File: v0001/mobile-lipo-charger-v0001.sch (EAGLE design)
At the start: 76 parts, among them IC1 AD8610MR, IC3 AD8610MR, IC5 STM32F429NGH, SW2 DHT-4235A, U3 3.3V, U4 3.3V

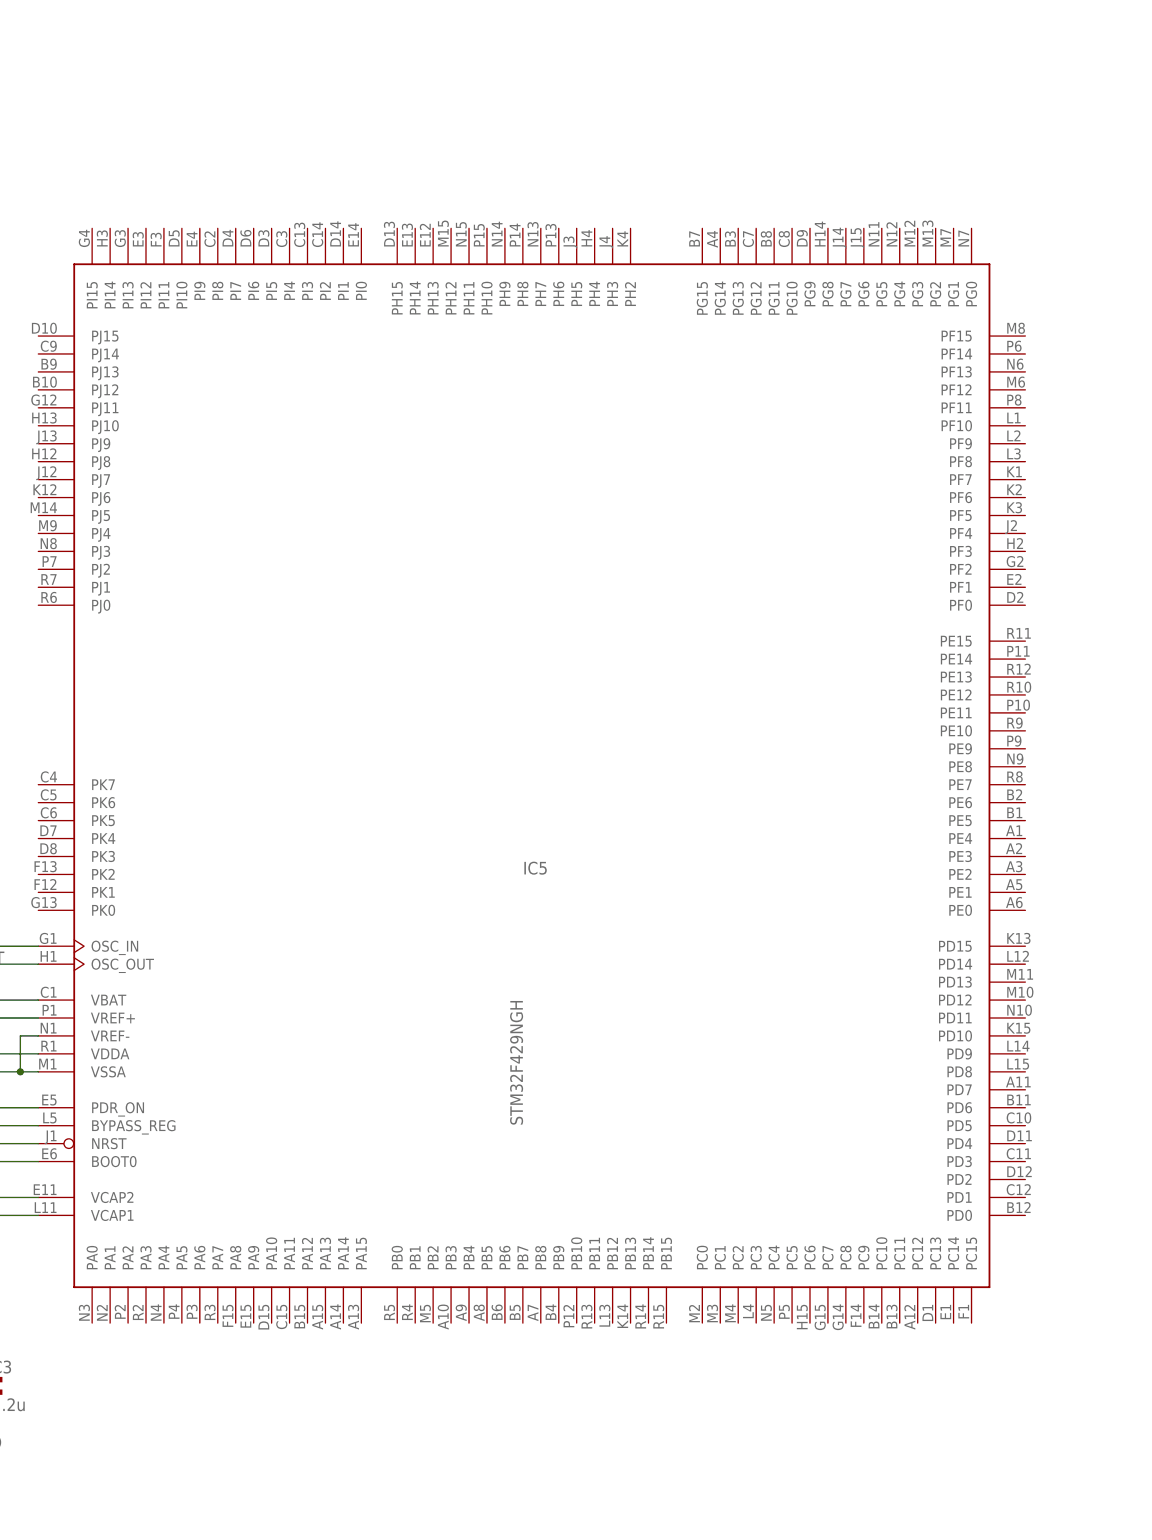
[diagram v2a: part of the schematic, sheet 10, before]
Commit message: Routing
Began routing TFT signals
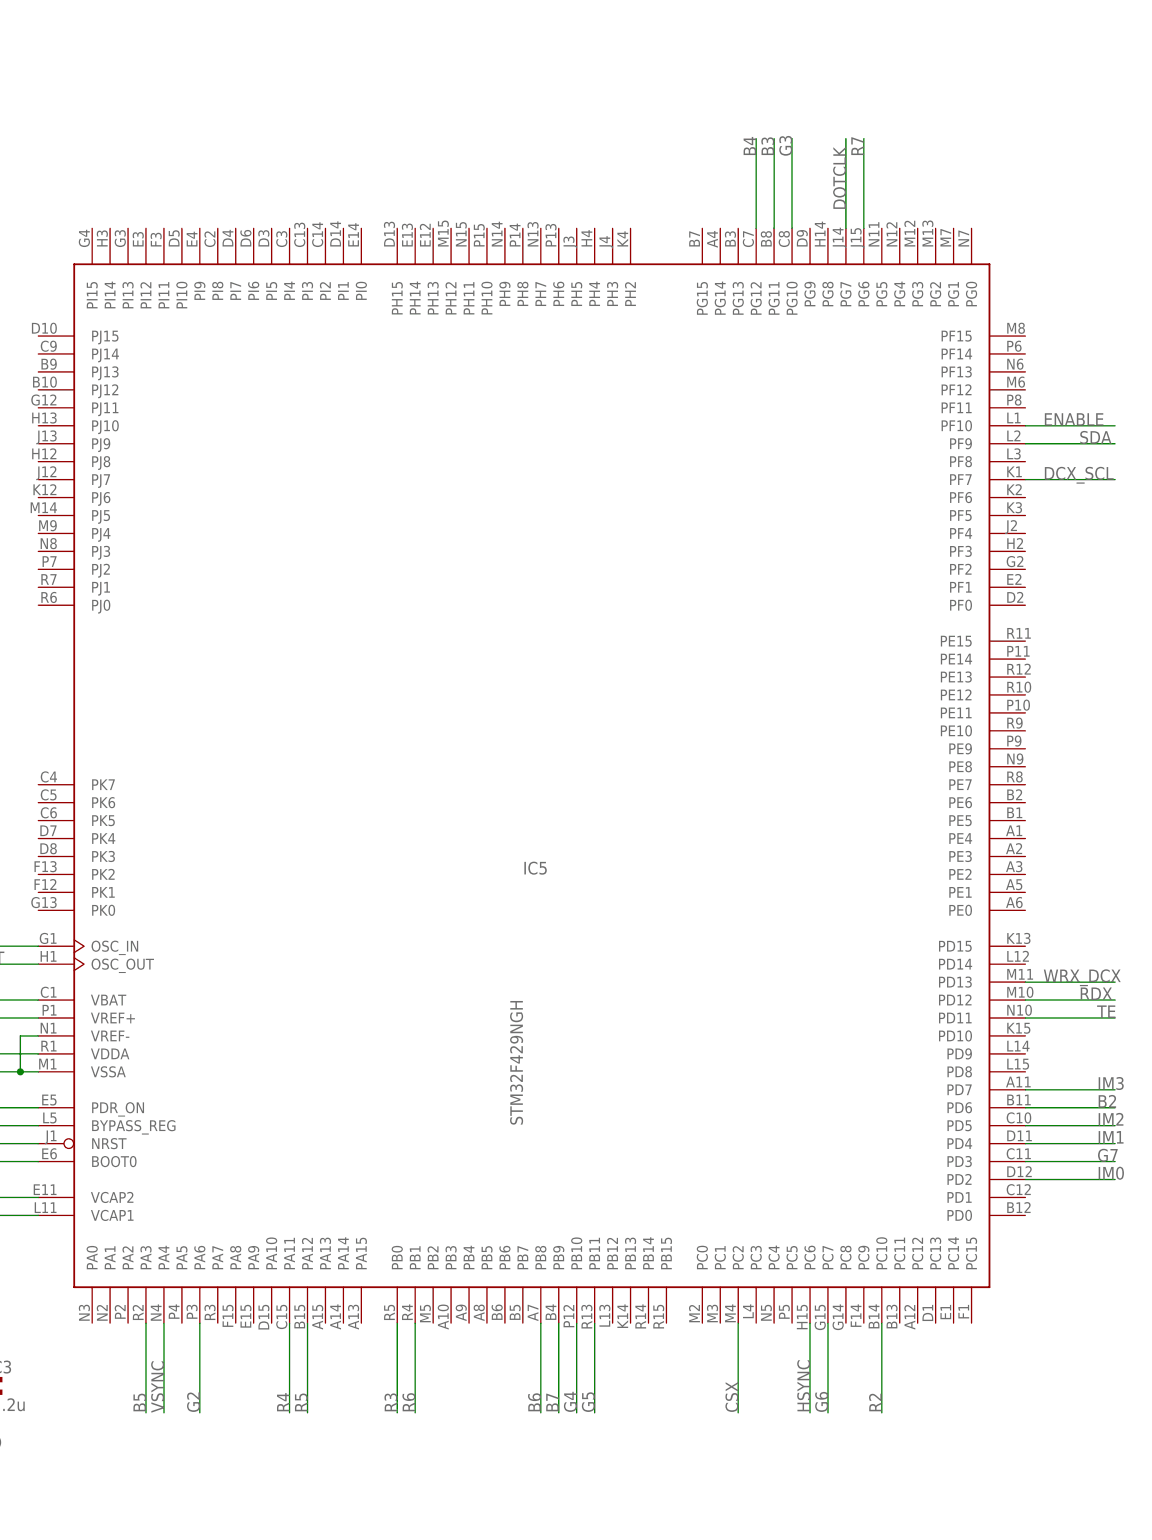
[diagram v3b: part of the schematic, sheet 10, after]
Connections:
- removed net TFT_CS#: J1.38
- removed net TFT_DB0: J1.32
- removed net TFT_DB1: J1.31
- removed net TFT_DB10: J1.22
- removed net TFT_DB11: J1.21
- removed net TFT_DB12: J1.20
- removed net TFT_DB13: J1.19
- removed net TFT_DB14: J1.18
- removed net TFT_DB15: J1.17
- removed net TFT_DB16: J1.16
- removed net TFT_DB17: J1.15
- removed net TFT_DB2: J1.30
- removed net TFT_DB3: J1.29
- removed net TFT_DB4: J1.28
- removed net TFT_DB5: J1.27
- removed net TFT_DB6: J1.26
- removed net TFT_DB7: J1.25
- removed net TFT_DB8: J1.24
- removed net TFT_DB9: J1.23
- removed net TFT_DE: J1.14
- removed net TFT_DOTCLK: J1.13
- removed net TFT_HSYNC: J1.12
- removed net TFT_IM0: J1.6
- removed net TFT_IM1: J1.7
- removed net TFT_IM2: J1.8
- removed net TFT_IM3: J1.9
- removed net TFT_RESET#: J1.10
- removed net TFT_RS_SCL: J1.37
- removed net TFT_SDI: J1.34
- removed net TFT_TE: J1.39
- removed net TFT_VSYNC: J1.11
- new net B2: IC5MCU.PD6, J1.32
- new net B3: IC5MCU.PG11, J1.31
- new net B4: IC5MCU.PG12, J1.30
- new net B5: IC5MCU.PA3, J1.29
- new net B6: IC5MCU.PB8, J1.28
- new net B7: IC5MCU.PB9, J1.27
- new net CSX: IC5MCU.PC2, J1.38
- new net DCX_SCL: IC5MCU.PF7, J1.37
- new net DOTCLK: IC5MCU.PG7, J1.13
- new net ENABLE: IC5MCU.PF10, J1.14
- new net G2: IC5MCU.PA6, J1.26
- new net G3: IC5MCU.PG10, J1.25
- new net G4: IC5MCU.PB10, J1.24
- new net G5: IC5MCU.PB11, J1.23
- new net G6: IC5MCU.PC7, J1.22
- new net G7: IC5MCU.PD3, J1.21
- new net HSYNC: IC5MCU.PC6, J1.12
- new net IM0: IC5MCU.PD2, J1.6
- new net IM1: IC5MCU.PD4, J1.7
- new net IM2: IC5MCU.PD5, J1.8
- new net IM3: IC5MCU.PD7, J1.9
- new net R2: IC5MCU.PC10, J1.20
- new net R3: IC5MCU.PB0, J1.19
- new net R4: IC5MCU.PA11, J1.18
- new net R5: IC5MCU.PA12, J1.17
- new net R6: IC5MCU.PB1, J1.16
- new net R7: IC5MCU.PG6, J1.15
- new net RDX: IC5MCU.PD12
- new net SDA: IC5MCU.PF9, J1.34
- new net TE: IC5MCU.PD11, J1.39
- new net VSYNC: IC5MCU.PA4, J1.11
- new net WRX_DCX: IC5MCU.PD13
- net RST: now also J1.10

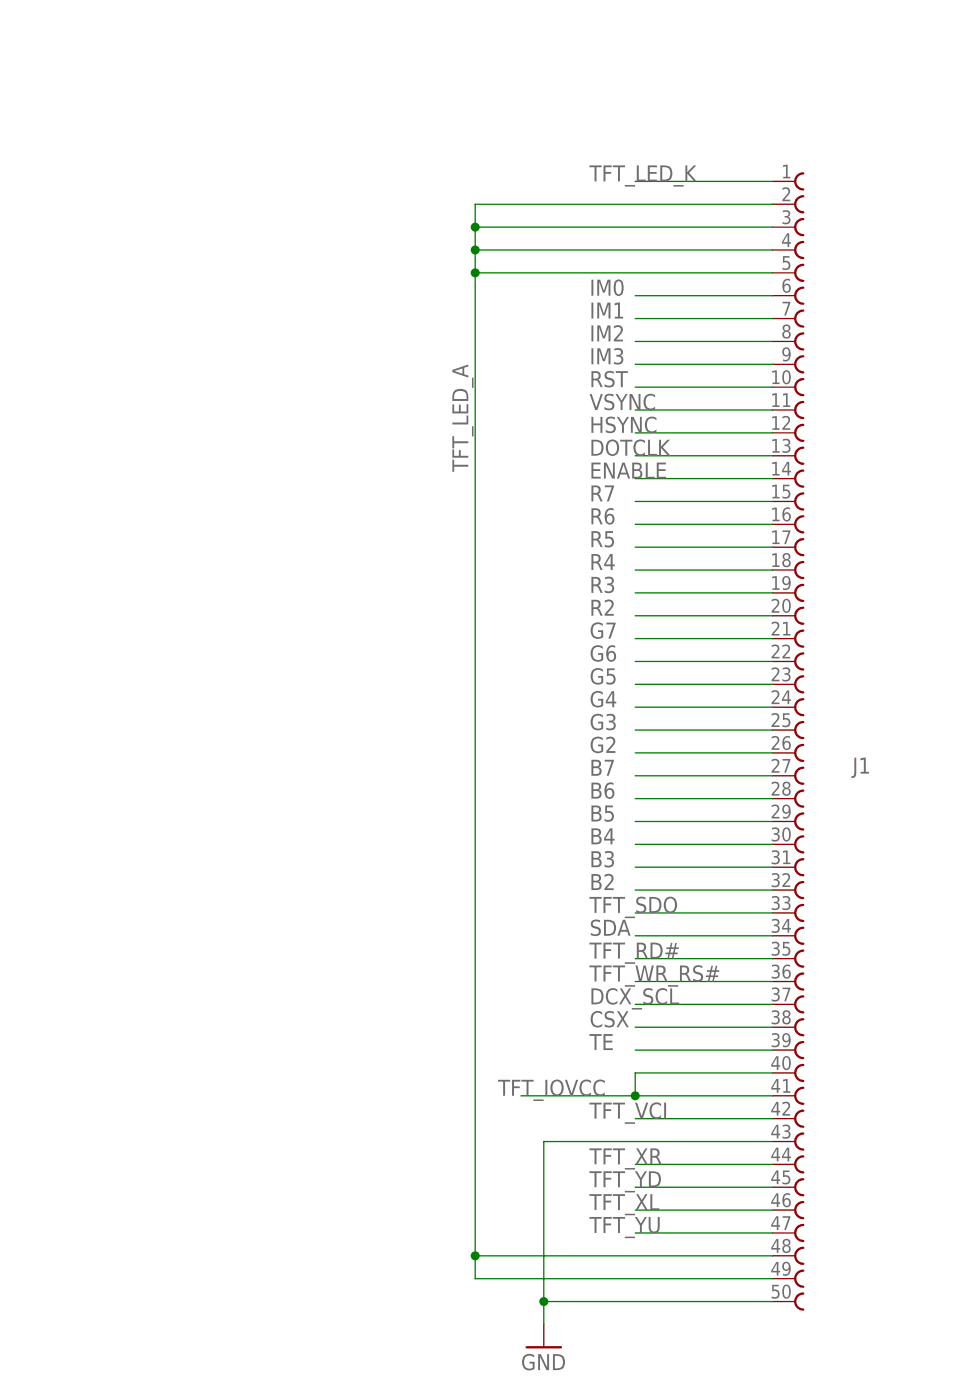
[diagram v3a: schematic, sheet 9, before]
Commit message: LED Backlight
Added the LCD backlight control and PSU
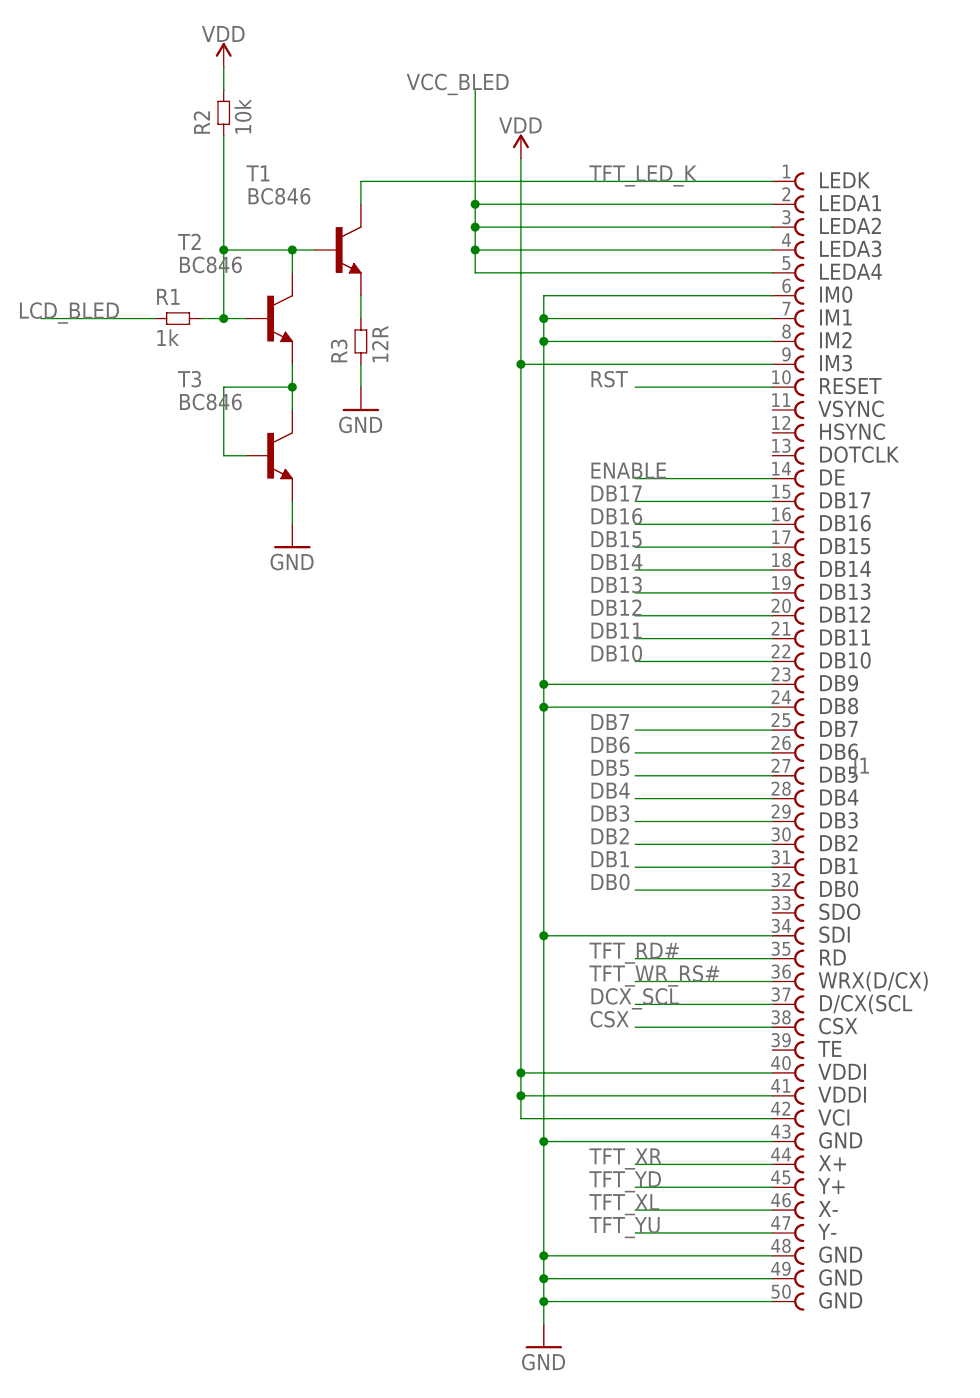
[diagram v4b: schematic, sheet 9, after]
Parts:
- added R1: 1k, common:RES0603L3
- added R2: 10k, common:RES0603L3
- added R3: 12R, common:RES0603L3
- added T1, T2, T3: BC846, transistor:BC846
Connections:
- removed net TFT_IOVCC: J1.40, J1.41
- removed net TFT_LED_A: J1.2, J1.3, J1.4, J1.48, J1.49, J1.5
- removed net TFT_SDO: J1.33
- removed net TFT_VCI: J1.42
- new net DB0: J1.32
- new net DB1: J1.31
- new net DB10: J1.22
- new net DB11: J1.21
- new net DB12: J1.20
- new net DB13: J1.19
- new net DB14: J1.18
- new net DB15: J1.17
- new net DB16: J1.16
- new net DB17: J1.15
- new net DB2: J1.30
- new net DB3: J1.29
- new net DB4: J1.28
- new net DB5: J1.27
- new net DB6: J1.26
- new net DB7: J1.25
- new net LCD_BLED: R1.1
- new net N$5: T2.E, T3.B, T3.C
- new net N$6: R3.2, T1.E
- new net N$7: R1.2, R2.1, T1.B, T2.B, T2.C
- new net VCC_BLED: J1.2, J1.3, J1.4, J1.5
- net B2: no longer J1.32
- net B3: no longer J1.31
- net B4: no longer J1.30
- net B5: no longer J1.29
- net B6: no longer J1.28
- net B7: no longer J1.27
- net DOTCLK: no longer J1.13
- net G2: no longer J1.26
- net G3: no longer J1.25
- net G4: no longer J1.24
- net G5: no longer J1.23
- net G6: no longer J1.22
- net G7: no longer J1.21
- net GND: now also J1.23, J1.24, J1.34, J1.48, J1.49, J1.6, J1.7, J1.8, R3.1, T3.E
- net HSYNC: no longer J1.12
- net IM0: no longer J1.6
- net IM1: no longer J1.7
- net IM2: no longer J1.8
- net IM3: no longer J1.9
- net R2: no longer J1.20
- net R3: no longer J1.19
- net R4: no longer J1.18
- net R5: no longer J1.17
- net R6: no longer J1.16
- net R7: no longer J1.15
- net SDA: no longer J1.34
- net TE: no longer J1.39
- net TFT_LED_K: now also T1.C
- net VDD: now also J1.40, J1.41, J1.42, J1.9, R2.2
- net VSYNC: no longer J1.11
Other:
- note added: "CSX"
- note added: "D/CX(SCL"
- note added: "DB0"
- note added: "DB1"
- note added: "DB10"
- note added: "DB11"
- note added: "DB12"
- note added: "DB13"
- note added: "DB14"
- note added: "DB15"
- note added: "DB16"
- note added: "DB17"
- note added: "DB2"
- note added: "DB3"
- note added: "DB4"
- note added: "DB5"
- note added: "DB6"
- note added: "DB7"
- note added: "DB8"
- note added: "DB9"
- note added: "DE"
- note added: "DOTCLK"
- note added: "GND"
- note added: "HSYNC"
- note added: "IM0"
- note added: "IM1"
- note added: "IM2"
- note added: "IM3"
- note added: "LEDA1"
- note added: "LEDA2"
- note added: "LEDA3"
- note added: "LEDA4"
- note added: "LEDK"
- note added: "RD"
- note added: "RESET"
- note added: "SDI"
- note added: "SDO"
- note added: "TE"
- note added: "VCI"
- note added: "VDDI"
- note added: "VSYNC"
- note added: "WRX(D/CX)"
- note added: "X+"
- note added: "X-"
- note added: "Y+"
- note added: "Y-"
